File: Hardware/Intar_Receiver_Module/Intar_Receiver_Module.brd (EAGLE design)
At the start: 17.8 x 25.9 mm, 13 parts, among them J1 GROVE-4P-2.0-3470130P1, U1 IR_RECEIVER

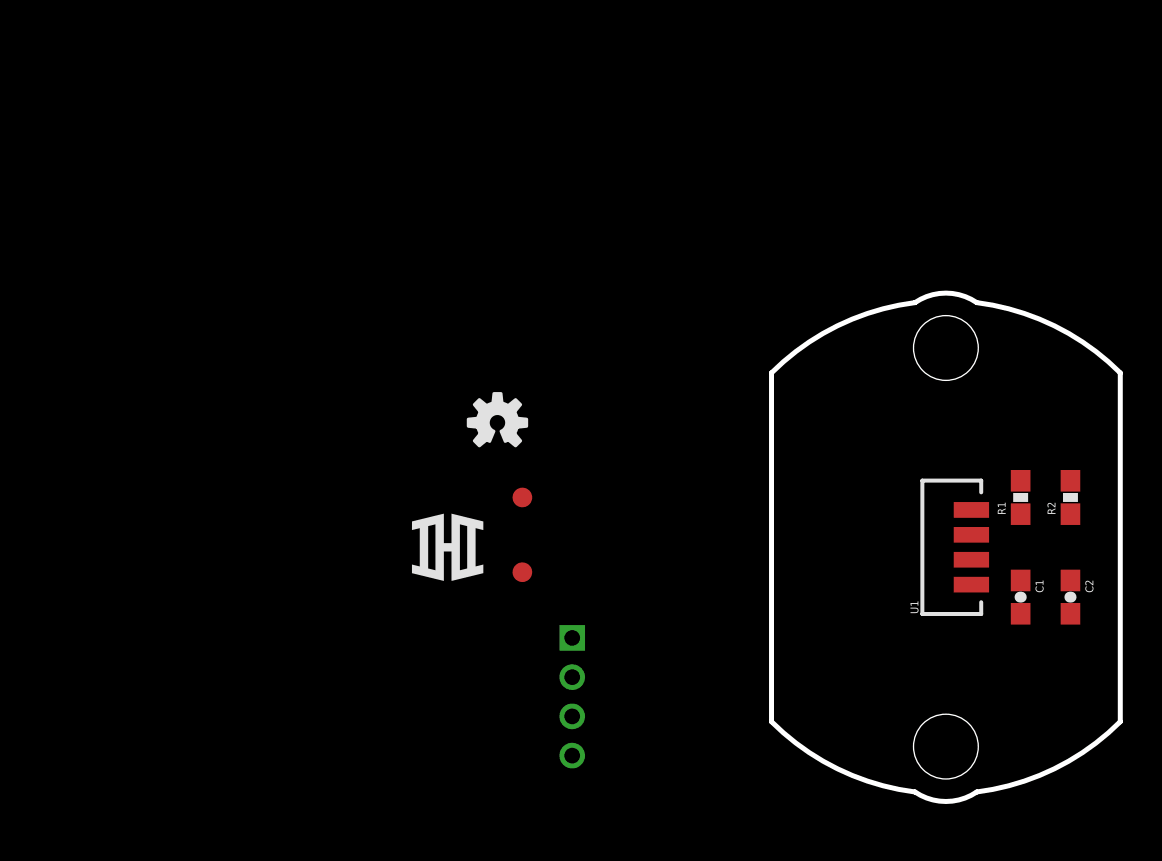
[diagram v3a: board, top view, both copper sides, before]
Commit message: Completed Vibration Module v01 layout
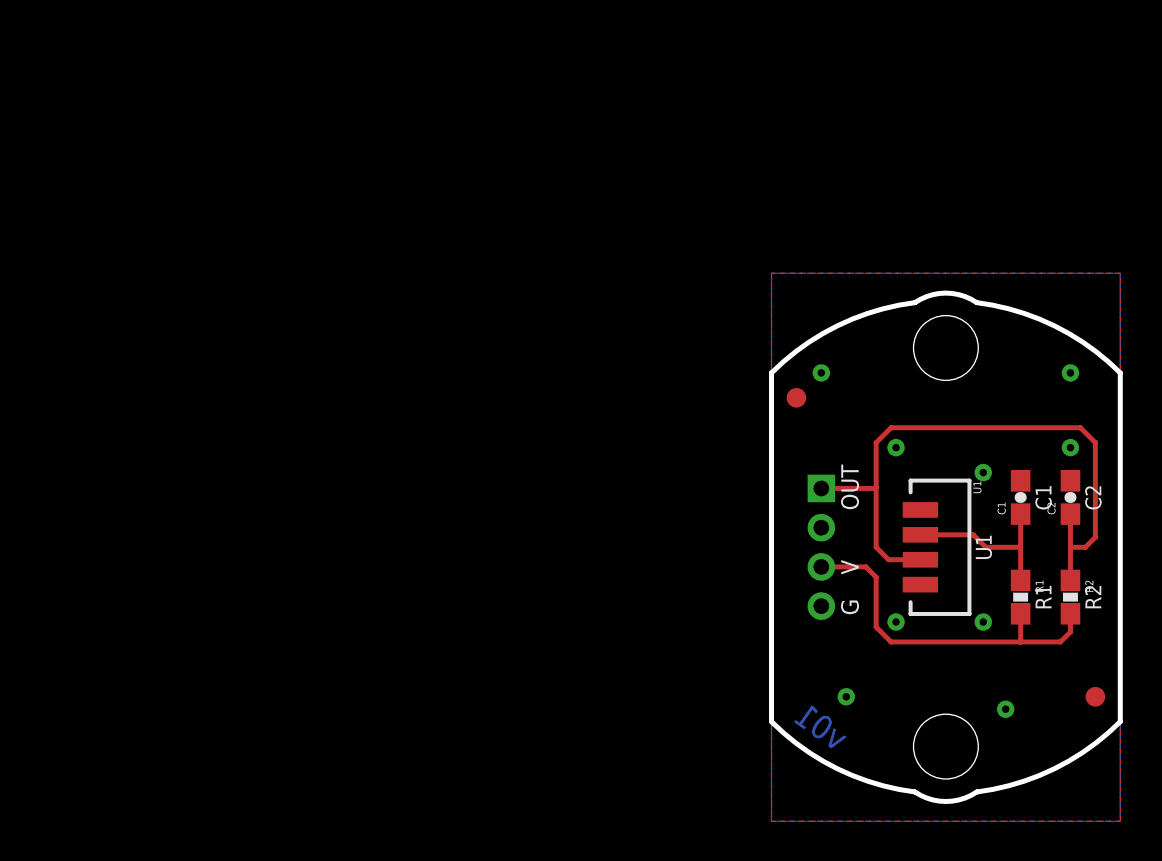
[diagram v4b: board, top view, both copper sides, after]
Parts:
- moved U$1 31.6 mm to (5.08, -8.26), flipped to the bottom, turned to 270 degrees
- moved FID2 29.9 mm to (7.62, -7.62)
- moved LOGO1 28.0 mm to (5.08, 8.26), flipped to the bottom, turned to 270 degrees
- moved FID1 14.9 mm to (-7.62, 7.62)
- moved J1 14.8 mm to (-6.35, 0.00)
- moved FRAME1 5.08 mm to (-33.0, -22.9)
- moved C1 5.08 mm to (3.81, 2.54), turned to 90 degrees
- moved C2 5.08 mm to (6.35, 2.54), turned to 90 degrees
- moved R1 5.08 mm to (3.81, -2.54), turned to 270 degrees
- moved R2 5.08 mm to (6.35, -2.54), turned to 270 degrees
- turned U1 to 270 degrees
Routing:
- net OUT: track 0.00 -> 32.2 mm
- net VCC: track 0.00 -> 18.3 mm
- net N$2: track 0.00 -> 8.75 mm
- added copper zone on layer 1, net GND
- added copper zone on layer 16, net GND
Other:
- board text added: "C1"
- board text added: "C2"
- board text added: "G"
- board text added: "Intar Receiver Module"
- board text added: "OUT"
- board text added: "R1"
- board text added: "R2"
- board text added: "Shawn Hymel"
- board text added: "U1"
- board text added: "V"
- board text added: "v01"

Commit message: Moved IHI and OSH logos away from name on all boards.
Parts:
- moved LOGO1 0.63 mm to (4.45, 8.26)
- moved U$1 0.63 mm to (4.45, -8.26)
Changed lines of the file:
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@@
 <setting verticaltext="up"/>
 </settings>
-<grid distance="0.05" unitdist="inch" unit="inch" style="dots" multiple="1" display="yes" altdistance="0.025" altunitdist="inch" altunit="inch"/>
+<grid distance="0.05" unitdist="inch" unit="inch" style="dots" multiple="1" display="yes" altdistance="0.005" altunitdist="inch" altunit="inch"/>
 <layers>
 <layer number="1" name="Top" color="4" fill="1" visible="yes" active="yes"/>
-<layer number="2" name="Route2" color="1" fill="3" visible="yes" active="yes"/>
-<layer number="15" name="Route15" color="4" fill="6" visible="yes" active="yes"/>
+<layer number="2" name="Route2" color="1" fill="3" visible="no" active="yes"/>
+<layer number="15" name="Route15" color="4" fill="6" visible="no" active="yes"/>
 <layer number="16" name="Bottom" color="1" fill="1" visible="yes" active="yes"/>
 <layer number="17" name="Pads" color="2" fill="1" visible="yes" active="yes"/>
@@
 <layer number="23" name="tOrigins" color="15" fill="1" visible="yes" active="yes"/>
 <layer number="24" name="bOrigins" color="15" fill="1" visible="yes" active="yes"/>
-<layer number="25" name="tNames" color="7" fill="1" visible="yes" active="yes"/>
-<layer number="26" name="bNames" color="7" fill="1" visible="yes" active="yes"/>
-<layer number="27" name="tValues" color="7" fill="1" visible="yes" active="yes"/>
-<layer number="28" name="bValues" color="7" fill="1" visible="yes" active="yes"/>
-<layer number="29" name="tStop" color="7" fill="3" visible="yes" active="yes"/>
-<layer number="30" name="bStop" color="7" fill="6" visible="yes" active="yes"/>
-<layer number="31" name="tCream" color="7" fill="4" visible="yes" active="yes"/>
-<layer number="32" name="bCream" color="7" fill="5" visible="yes" active="yes"/>
-<layer number="39" name="tKeepout" color="4" fill="11" visible="yes" active="yes"/>
-<layer number="40" name="bKeepout" color="1" fill="11" visible="yes" active="yes"/>
-<layer number="41" name="tRestrict" color="4" fill="10" visible="yes" active="yes"/>
-<layer number="42" name="bRestrict" color="1" fill="10" visible="yes" active="yes"/>
-<layer number="43" name="vRestrict" color="2" fill="10" visible="yes" active="yes"/>
-<layer number="44" name="Drills" color="7" fill="1" visible="yes" active="yes"/>
+<layer number="25" name="tNames" color="7" fill="1" visible="no" active="yes"/>
+<layer number="26" name="bNames" color="7" fill="1" visible="no" active="yes"/>
+<layer number="27" name="tValues" color="7" fill="1" visible="no" active="yes"/>
+<layer number="28" name="bValues" color="7" fill="1" visible="no" active="yes"/>
+<layer number="29" name="tStop" color="7" fill="3" visible="no" active="yes"/>
+<layer number="30" name="bStop" color="7" fill="6" visible="no" active="yes"/>
+<layer number="31" name="tCream" color="7" fill="4" visible="no" active="yes"/>
+<layer number="32" name="bCream" color="7" fill="5" visible="no" active="yes"/>
+<layer number="39" name="tKeepout" color="4" fill="11" visible="no" active="yes"/>
+<layer number="40" name="bKeepout" color="1" fill="11" visible="no" active="yes"/>
+<layer number="41" name="tRestrict" color="4" fill="10" visible="no" active="yes"/>
+<layer number="42" name="bRestrict" color="1" fill="10" visible="no" active="yes"/>
+<layer number="43" name="vRestrict" color="2" fill="10" visible="no" active="yes"/>
+<layer number="44" name="Drills" color="7" fill="1" visible="no" active="yes"/>
 <layer number="45" name="Holes" color="7" fill="1" visible="yes" active="yes"/>
-<layer number="46" name="Milling" color="3" fill="1" visible="yes" active="yes"/>
+<layer number="46" name="Milling" color="3" fill="1" visible="no" active="yes"/>
 <layer number="47" name="Measures" color="7" fill="1" visible="yes" active="yes"/>
 <layer number="51" name="tDocu" color="6" fill="1" visible="yes" active="yes"/>
-<layer number="52" name="bDocu" color="7" fill="1" visible="yes" active="yes"/>
+<layer number="52" name="bDocu" color="7" fill="1" visible="no" active="yes"/>
 <layer number="3" name="Route3" color="4" fill="3" visible="no" active="no"/>
 <layer number="4" name="Route4" color="1" fill="4" visible="no" active="no"/>
@@
 <element name="FID2" library="SparkFun-Aesthetics" package="FIDUCIAL-1X2" value="FIDUCIAL1X2" x="7.62" y="-7.62"/>
 <element name="FRAME1" library="SparkFun-Aesthetics" package="CREATIVE_COMMONS" value="FRAME-LETTER" x="-33.02" y="-22.86"/>
-<element name="LOGO1" library="SparkFun-Aesthetics" package="OSHW-LOGO-S" value="OSHW-LOGOS" x="5.08" y="8.255" rot="MR270"/>
+<element name="LOGO1" library="SparkFun-Aesthetics" package="OSHW-LOGO-S" value="OSHW-LOGOS" x="4.445" y="8.255" rot="MR270"/>
 <element name="R1" library="SparkFun-Resistors" package="0603-RES" value="100" x="3.81" y="-2.54" rot="R270">
 <attribute name="PROD_ID" value="RES-07863" x="3.81" y="-2.54" size="1.778" layer="27" rot="R270" display="off"/>
@@
 <element name="STANDOFF1" library="SparkFun-Electromechanical" package="STAND-OFF" value="STAND-OFF" x="0" y="-10.16"/>
 <element name="STANDOFF2" library="SparkFun-Electromechanical" package="STAND-OFF" value="STAND-OFF" x="0" y="10.16"/>
-<element name="U$1" library="Intar_Eagle_Library" package="LOGO_SM" value="LOGOSM" x="5.08" y="-8.255" rot="MR270"/>
+<element name="U$1" library="Intar_Eagle_Library" package="LOGO_SM" value="LOGOSM" x="4.445" y="-8.255" rot="MR270"/>
 <element name="U1" library="Intar_Eagle_Library" package="TSOP754XXW" value="IR_RECEIVER" x="0" y="0" rot="R270"/>
 <element name="J1" library="Connector" package="4P-2.0" value="GROVE-4P-2.0-3470130P1" x="-6.35" y="0" rot="MR270"/>
